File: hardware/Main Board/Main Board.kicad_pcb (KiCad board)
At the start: 2 copper layers, 65 x 56 mm, 12 parts, among them J1 Daughter Board Connector, J2 ATtiny84 I2C/SPI Debug, J3 ATtiny85 I2c/SPI Debug, P1 Raspberry Pi, U1 ATtiny84-20PU, U2 ATtiny85-20PU

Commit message: The New (v2) Board
Signed-off-by: John Jacques <eruditelite@gmail.com>
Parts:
- added C1: 100nF, Capacitor_THT:C_Disc_D5.0mm_W2.5mm_P2.50mm, F.Cu at (204.0, 111.2)
- added C2: 100nF, Capacitor_THT:C_Disc_D5.0mm_W2.5mm_P2.50mm, F.Cu at (252.8, 122.8)
- added C3: 47uF, Capacitor_THT:CP_Radial_D6.3mm_P2.50mm, F.Cu at (230.8, 102.8)
- added C4: 100nF, Capacitor_THT:C_Disc_D5.0mm_W2.5mm_P2.50mm, F.Cu at (261.8, 110.5)
- added SW1: SW_DIP_x02, Button_Switch_THT:SW_DIP_SPSTx02_Slide_9.78x7.26mm_W7.62mm_P2.54mm, F.Cu at (245.3, 142.2)
- added U3: 74HC125, Package_DIP:DIP-14_W7.62mm_Socket, F.Cu at (257.2, 105.8)
- J1: value Daughter Board Connector -> Conn_02x13_Odd_Even; footprint Connector_PinSocket_2.54mm:PinSocket_2x10_P2.54mm_Vertical -> Connector_PinSocket_2.00mm:PinSocket_2x13_P2.00mm_Vertical
- J2: value ATtiny84 I2C/SPI Debug -> ATTiny84 Debug; footprint Connector_PinHeader_2.54mm:PinHeader_1x03_P2.54mm_Vertical -> Connector_PinHeader_1.27mm:PinHeader_1x13_P1.27mm_Vertical
- J3: value ATtiny85 I2c/SPI Debug -> ATTiny85 Debug; footprint Connector_PinHeader_2.54mm:PinHeader_1x03_P2.54mm_Vertical -> Connector_PinHeader_1.27mm:PinHeader_1x07_P1.27mm_Vertical
- R1, R2: value 1K -> 10K; footprint Resistor_THT:R_Axial_DIN0207_L6.3mm_D2.5mm_P7.62mm_Horizontal -> Resistor_THT:R_Axial_DIN0204_L3.6mm_D1.6mm_P2.54mm_Vertical
- moved R2 29.9 mm to (243.0, 120.7), turned to 270 degrees
- moved J1 23.0 mm to (227.0, 119.0), turned to 0 degrees
- moved J3 17.3 mm to (262.5, 124.8)
- moved R1 17.0 mm to (203.0, 117.0), turned to 270 degrees
- moved J2 10.5 mm to (202.5, 125.0)
- moved U2 9.54 mm to (245.2, 125.9)
- moved U1 7.48 mm to (209.0, 110.8)
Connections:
- J1 pad 1: /GPIO10(SPI0_MOSI) -> +3V3
- J1 pad 10: /GPIO2(SDA1) -> 84_PA1
- J1 pad 11: Net-(J1-Pad11) -> 84_PB1
- J1 pad 12: /GPIO19(SPI1_MISO) -> 84_PA2
- J1 pad 13: Net-(J1-Pad13) -> 84_PB3
- J1 pad 14: /GPIO21(SPI1_SCK) -> 84_PA3
- J1 pad 15: Net-(J1-Pad15) -> 84_PB2
- J1 pad 16: Net-(J1-Pad16) -> 84_PA4
- J1 pad 17: Net-(J1-Pad17) -> 85_PB5
- J1 pad 18: Net-(J1-Pad18) -> 84_PA5
- J1 pad 19: +5V -> 85_PB3
- J1 pad 2: GND -> +5V
- J1 pad 20: +3V3 -> 84_PA7
- J1 pad 3: Net-(J1-Pad3) -> /GPIO20(SPI1_MOSI)
- J1 pad 4: GND -> /ID_SC
- J1 pad 5: Net-(J1-Pad5) -> /GPIO21(SPI1_SCK)
- J1 pad 6: Net-(J1-Pad6) -> /ID_SD
- J1 pad 7: /GPIO9(SPI0_MISO) -> /GPIO26
- J1 pad 8: Net-(J1-Pad8) -> 84_PA0
- J1 pad 9: /GPIO11(SPI0_SCK) -> 84_PB0
- J2 pad 1: /GPIO11(SPI0_SCK) -> GND
- J2 pad 2: /GPIO9(SPI0_MISO) -> 84_PB0
- J2 pad 3: /GPIO10(SPI0_MOSI) -> 84_PB1
- J3 pad 1: /GPIO21(SPI1_SCK) -> GND
- J3 pad 2: /GPIO19(SPI1_MISO) -> 85_PB2
- J3 pad 3: /GPIO2(SDA1) -> 85_PB1
- P1 pad 13: /GPIO27(GEN2) -> 84_PB3
- P1 pad 27: /GPIO10(SPI0_MOSI) -> /ID_SD
- P1 pad 28: /GPIO11(SPI0_SCK) -> /ID_SC
- P1 pad 3: /GPIO2(SDA1) -> 84_PA6
- P1 pad 38: /GPIO2(SDA1) -> /GPIO20(SPI1_MOSI)
- P1 pad 5: /GPIO21(SPI1_SCK) -> 84_PA4
- P1 pad 7: /GPIO4(GCLK) -> 85_PB5
- P1 pad 9: Net-(P1-Pad9) -> GND
- R1 pad 2: /GPIO10(SPI0_MOSI) -> 84_PB3
- R2 pad 2: /GPIO11(SPI0_SCK) -> 85_PB5
- U1 pad 10: Net-(J1-Pad11) -> 84_PA3
- U1 pad 11: Net-(J1-Pad13) -> 84_PA2
- U1 pad 12: Net-(J1-Pad15) -> 84_PA1
- U1 pad 13: Net-(J1-Pad17) -> 84_PA0
- U1 pad 2: Net-(J1-Pad8) -> 84_PB0
- U1 pad 3: Net-(J1-Pad6) -> 84_PB1
- U1 pad 4: /GPIO22(GEN3) -> 84_PB3
- U1 pad 5: Net-(J1-Pad5) -> 84_PB2
- U1 pad 6: Net-(J1-Pad3) -> 84_PA7
- U1 pad 7: /GPIO10(SPI0_MOSI) -> 84_PA6
- U1 pad 8: /GPIO9(SPI0_MISO) -> 84_PA5
- U1 pad 9: /GPIO11(SPI0_SCK) -> 84_PA4
- U2 pad 1: /GPIO22(GEN3) -> 85_PB5
- U2 pad 2: Net-(J1-Pad18) -> 85_PB3
- U2 pad 3: Net-(J1-Pad16) -> 85_PB4
- U2 pad 5: /GPIO2(SDA1) -> 85_PB0
- U2 pad 6: /GPIO19(SPI1_MISO) -> 85_PB1
- U2 pad 7: /GPIO21(SPI1_SCK) -> 85_PB2
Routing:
- net 84_PA4: track 0.00 -> 166.8 mm, vias 0 -> 1
- net 84_PA6: track 0.00 -> 145.0 mm, vias 0 -> 1
- net /GPIO2(SDA1): track 113.9 -> 0.00 mm
- net 85_PB5: track 0.00 -> 98.1 mm
- net 84_PB3: track 0.00 -> 75.9 mm
- net /GPIO10(SPI0_MOSI): track 94.6 -> 18.7 mm
- net 85_PB1: track 0.00 -> 69.2 mm, vias 0 -> 2
- net /GPIO22(GEN3): track 66.7 -> 0.00 mm
- net /GPIO14(TXD0): track 0.00 -> 65.2 mm
- net 84_PA5: track 0.00 -> 65.1 mm
- net /GPIO19(SPI1_MISO): track 60.1 -> 0.00 mm
- net /GPIO15(RXD0): track 0.00 -> 59.7 mm
- net /GPIO11(SPI0_SCK): track 80.2 -> 21.5 mm
- net 85_PB0: track 0.00 -> 51.8 mm
- net 85_PB2: track 0.00 -> 51.2 mm, vias 0 -> 1
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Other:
- outline, holes or cut-outs redrawn
- board text added: "ATTiny84/ATTiny85 Experiment Board"
- board text added: "RASPBERRY-PI 40-PIN ADDON BOARD VIEW FROM TOP NOTE: P1 SHOULD BE FITTED ON THE REVERSE OF THE BOARD ADD EDGE CUTS FROM CAMERA AND DISPLAY PORTS AS REQUIRED"
- board text added: "RJ45"
- board text added: "USB"
- board text added: "https://github.com/eruditelite/attiny"
- board text added: "release_2_0"
- board text removed: "ATTiny Examples eruditelite@gmail.com"
- board text removed: "CAMERA"
- board text removed: "Clock"
- board text removed: "DISPLAY"
- board text removed: "MISO"
- board text removed: "SDA/MOSI"

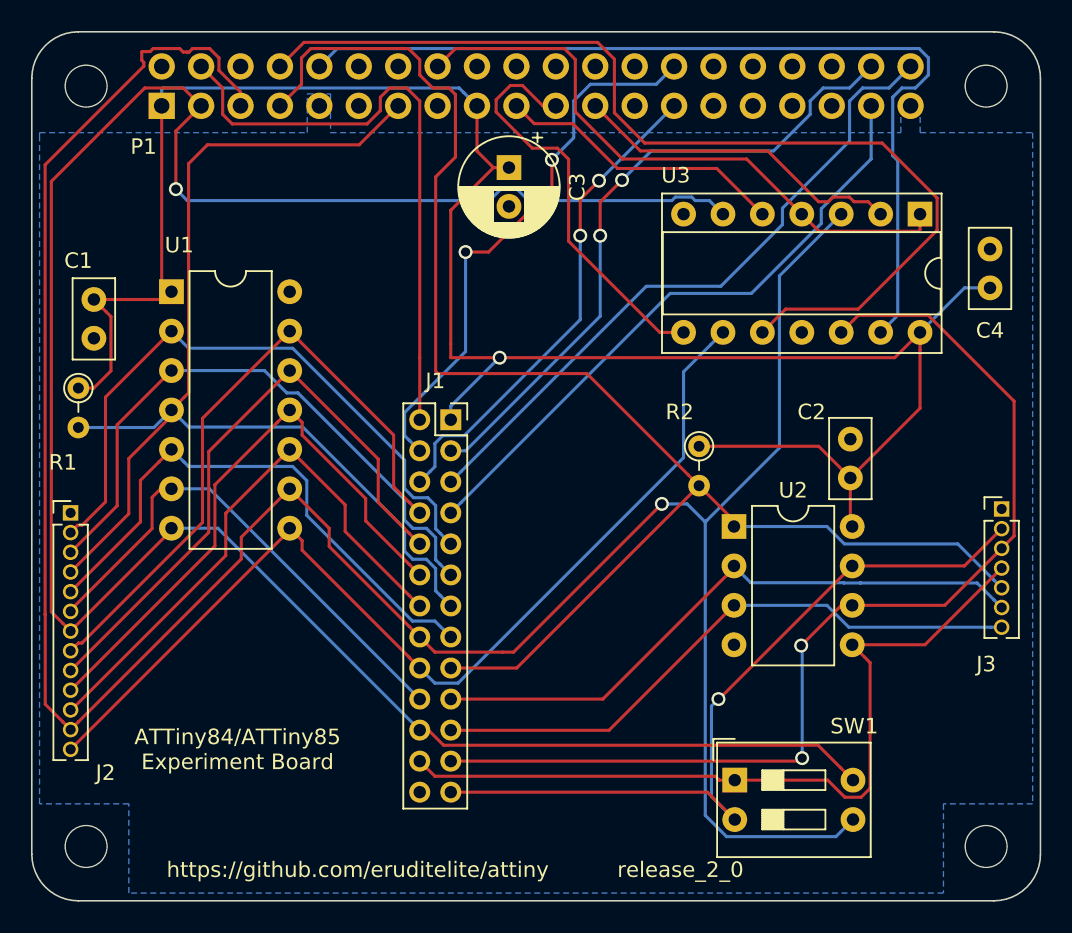
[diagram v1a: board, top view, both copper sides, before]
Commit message: Fix an Error in the v2 Board
The custom footprint for the quad buffer had two pin 12s!
Updated the silk to release_2_1 as well.

Signed-off-by: John Jacques <eruditelite@gmail.com>
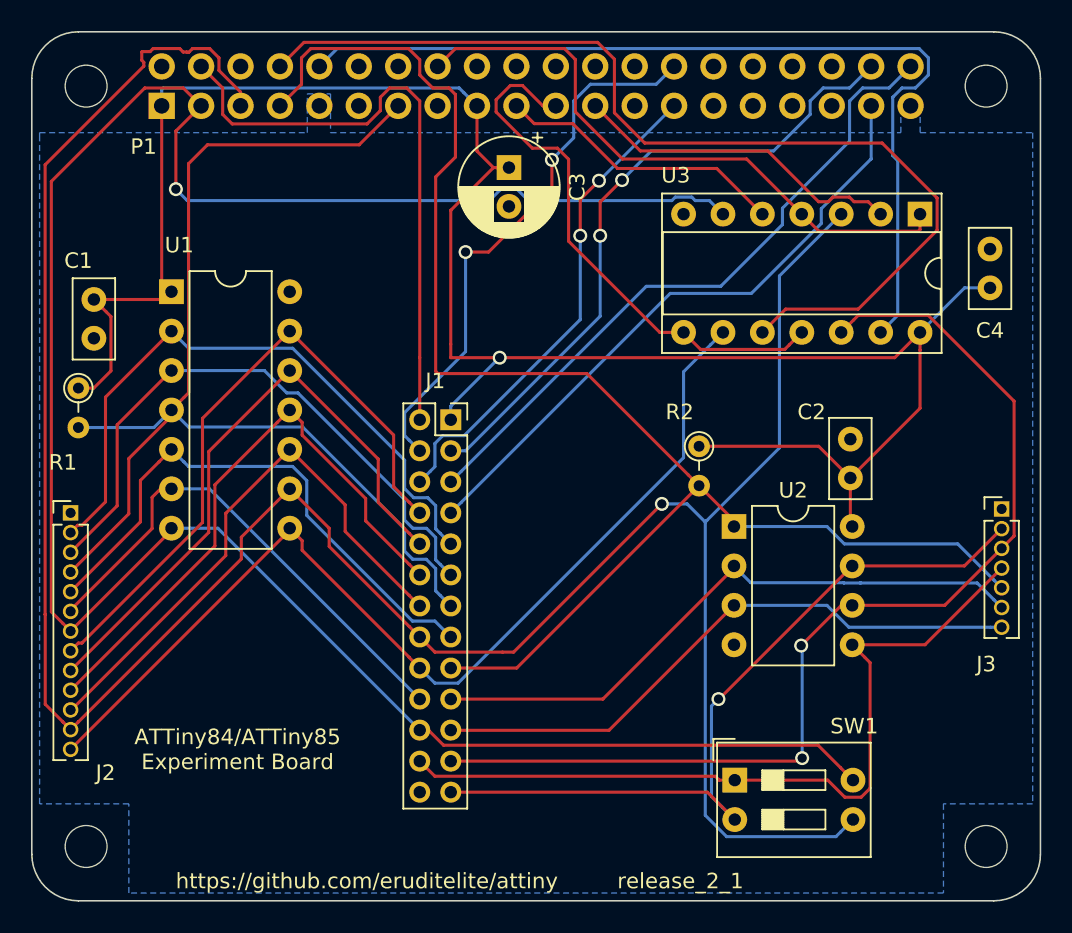
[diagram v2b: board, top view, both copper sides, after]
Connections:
- U3 pad 11: (no net) -> /GPIO9(SPI0_MISO)
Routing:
- net /GPIO9(SPI0_MISO): track 26.6 -> 35.1 mm
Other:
- board text added: "release_2_1"
- board text removed: "release_2_0"
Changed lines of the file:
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@@
-(kicad_pcb (version 20171130) (host pcbnew 5.1.0-060a0da~80~ubuntu18.04.1)
+(kicad_pcb (version 20171130) (host pcbnew 5.0.2-bee76a0~70~ubuntu18.04.1)
   (general
     (thickness 1.6)
     (drawings 27)
-    (tracks 456)
+    (tracks 460)
     (zones 0)
     (modules 18)
@@
     (43 Eco2.User user)
     (44 Edge.Cuts user)
+    (45 Margin user)
+    (46 B.CrtYd user)
+    (47 F.CrtYd user)
+    (48 B.Fab user)
+    (49 F.Fab user)
   )
   (setup
@@
     (zone_45_only no)
     (trace_min 0.1524)
+    (segment_width 0.1)
+    (edge_width 0.1)
     (via_size 0.9)
     (via_drill 0.6)
@@
     (uvia_min_size 0.5)
     (uvia_min_drill 0.1)
-    (edge_width 0.1)
-    (segment_width 0.1)
     (pcb_text_width 0.3)
     (pcb_text_size 1 1)
@@
     (pad_drill 2.5)
     (pad_to_mask_clearance 0)
+    (solder_mask_min_width 0.25)
     (aux_axis_origin 200 150)
     (grid_origin 200 150)
-    (visible_elements 7FFFFFFF)
+    (visible_elements 7FFFEFFF)
     (pcbplotparams
       (layerselection 0x00030_80000001)
@@
     (pad 4 thru_hole oval (at 0 7.62 270) (size 1.6 1.6) (drill 0.8) (layers *.Cu *.Mask)
       (net 8 "/GPIO23(GEN4)"))
-    (pad 11 thru_hole oval (at 7.62 7.62 270) (size 1.6 1.6) (drill 0.8) (layers *.Cu *.Mask))
+    (pad 11 thru_hole oval (at 7.62 7.62 270) (size 1.6 1.6) (drill 0.8) (layers *.Cu *.Mask)
+      (net 44 "/GPIO9(SPI0_MISO)"))
     (pad 5 thru_hole oval (at 0 10.16 270) (size 1.6 1.6) (drill 0.8) (layers *.Cu *.Mask)
       (net 48 "/GPIO10(SPI0_MOSI)"))
@@
     (effects (font (size 1 1) (thickness 0.15)))
   )
-  (gr_text release_2_0 (at 241.8 148) (layer F.SilkS)
+  (gr_text release_2_1 (at 241.8 148.73) (layer F.SilkS)
     (effects (font (size 1 1) (thickness 0.15)))
   )
-  (gr_text https://github.com/eruditelite/attiny (at 221 148) (layer F.SilkS)
+  (gr_text https://github.com/eruditelite/attiny (at 221.59 148.73) (layer F.SilkS)
     (effects (font (size 1 1) (thickness 0.15)))
   )
@@
   (segment (start 231.622102 97.4601) (end 230.837898 97.4601) (width 0.2) (layer F.Cu) (net 44))
   (segment (start 230.837898 97.4601) (end 229.9212 98.376798) (width 0.2) (layer F.Cu) (net 44))
+  (segment (start 248.519999 114.470001) (end 248.820001 114.169999) (width 0.2) (layer F.Cu) (net 44))
+  (segment (start 243.100001 114.470001) (end 248.519999 114.470001) (width 0.2) (layer F.Cu) (net 44))
+  (segment (start 248.820001 114.169999) (end 249.62 113.37) (width 0.2) (layer F.Cu) (net 44))
+  (segment (start 242 113.37) (end 243.100001 114.470001) (width 0.2) (layer F.Cu) (net 44))
   (segment (start 252.688001 104.649999) (end 252.988003 104.950001) (width 0.2) (layer F.Cu) (net 45))
   (segment (start 239.2165 101.6765) (end 247.4265 101.6765) (width 0.2) (layer F.Cu) (net 45))
